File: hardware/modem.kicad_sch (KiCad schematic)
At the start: 33 parts, among them J11 PRPC001DAAN-RC, Q2 IRLML2246TRPBF, Q3 MMBT3904, U7 74AVC1T45DW-7, U8 74AVC1T45DW-7, U9 SARA-R500S-61B

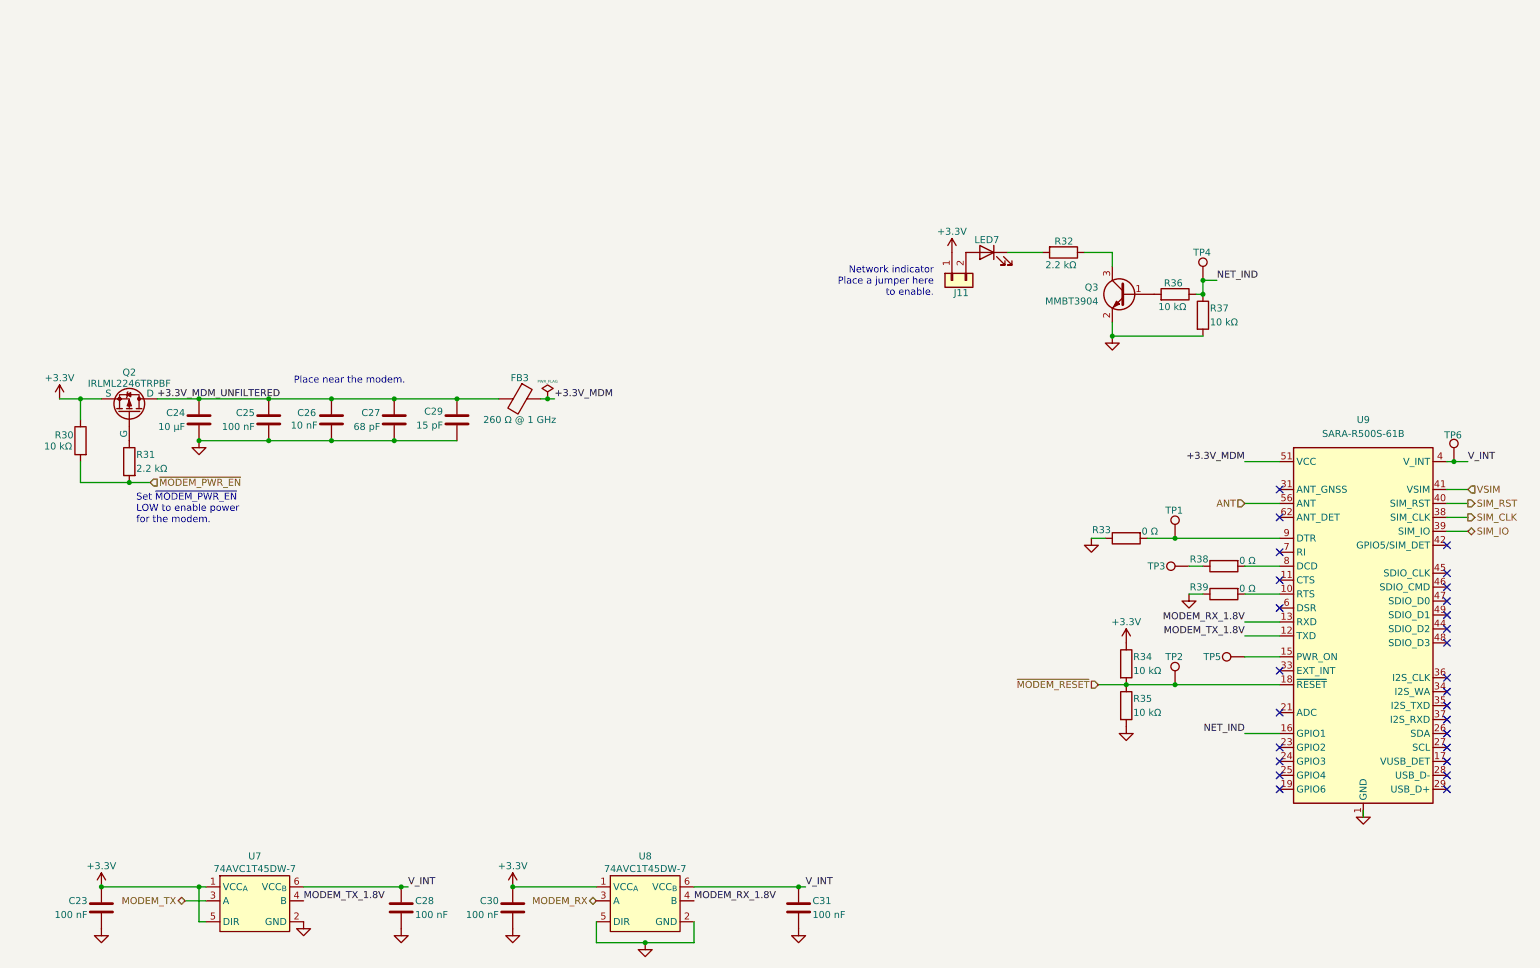
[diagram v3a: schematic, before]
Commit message: HW: Update components, change footprints to handsolder versions, finish power
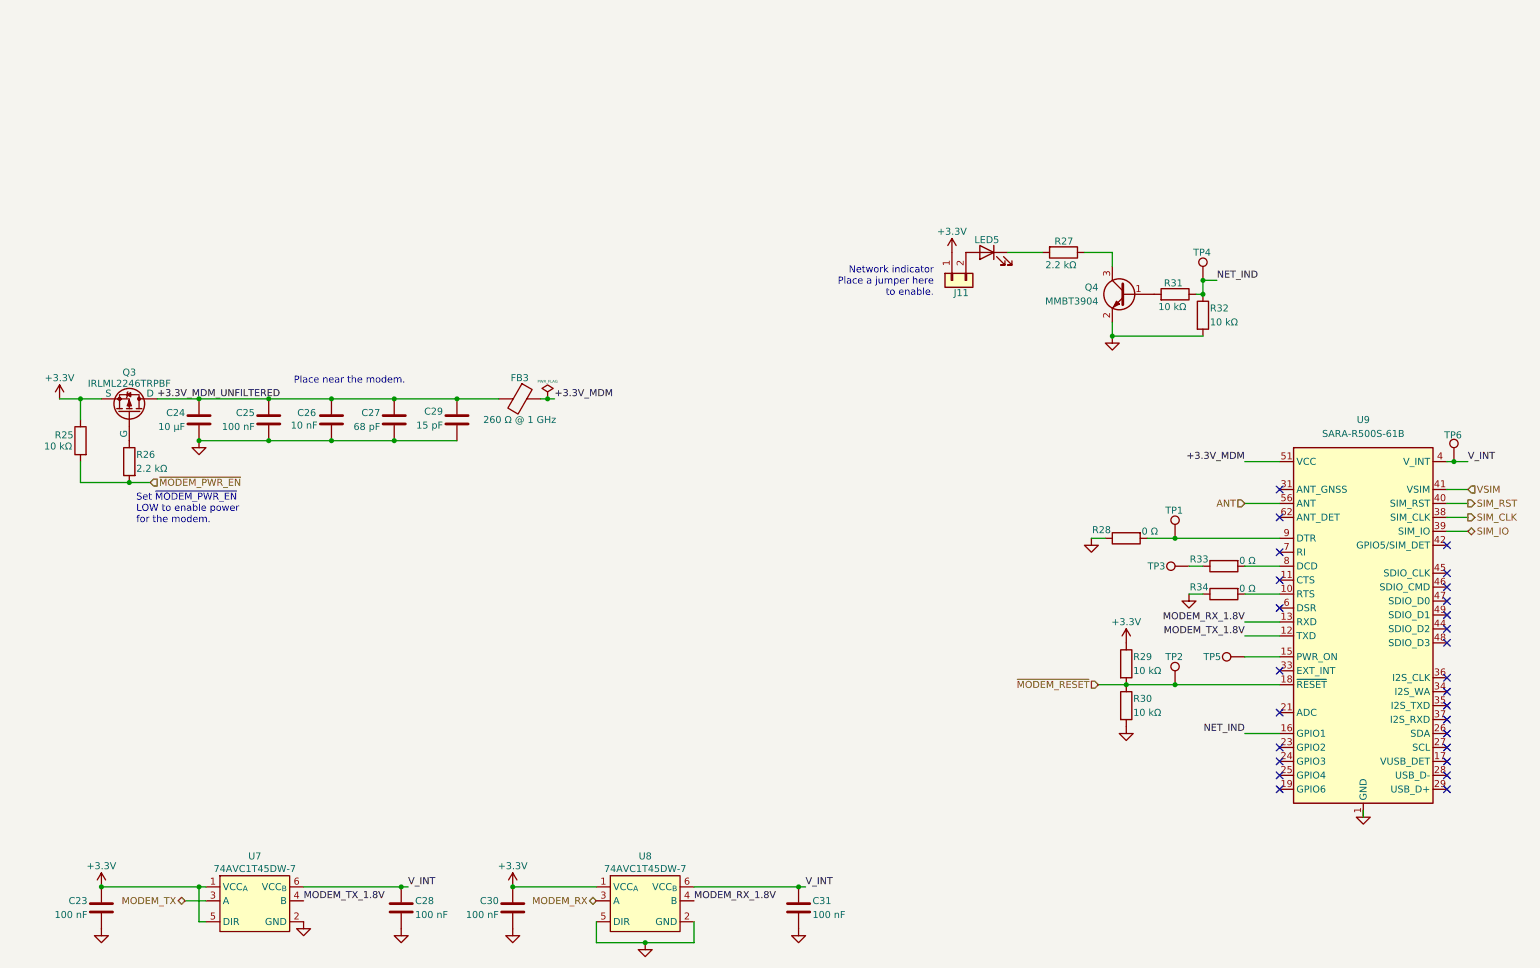
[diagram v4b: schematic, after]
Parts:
- R25: renamed from R30; Digi-Key Part Number 311-10.0KLRCT-ND -> 732-560112110020CT-ND; Manufacturer YAGEO -> Würth Elektronik; Manufacturer Part Number RC0402FR-0710KL -> 560112110020
- R26: renamed from R31; Digi-Key Part Number 311-2.20KLRCT-ND -> 732-560112110087CT-ND; Manufacturer YAGEO -> Würth Elektronik; Manufacturer Part Number RC0402FR-072K2L -> 560112110087
- R27: renamed from R32; Digi-Key Part Number 311-2.20KLRCT-ND -> 732-560112110087CT-ND; Manufacturer YAGEO -> Würth Elektronik; Manufacturer Part Number RC0402FR-072K2L -> 560112110087
- R28: renamed from R33; Digi-Key Part Number 311-0.0JRCT-ND -> 732-560112110001CT-ND; Manufacturer YAGEO -> Würth Elektronik; Manufacturer Part Number RC0402JR-070RL -> 560112110001
- R29: renamed from R34; Digi-Key Part Number 311-10.0KLRCT-ND -> 732-560112110020CT-ND; Manufacturer YAGEO -> Würth Elektronik; Manufacturer Part Number RC0402FR-0710KL -> 560112110020
- R30: renamed from R35; Digi-Key Part Number 311-10.0KLRCT-ND -> 732-560112110020CT-ND; Manufacturer YAGEO -> Würth Elektronik; Manufacturer Part Number RC0402FR-0710KL -> 560112110020
- R31: renamed from R36; Digi-Key Part Number 311-10.0KLRCT-ND -> 732-560112110020CT-ND; Manufacturer YAGEO -> Würth Elektronik; Manufacturer Part Number RC0402FR-0710KL -> 560112110020
- R32: renamed from R37; Digi-Key Part Number 311-10.0KLRCT-ND -> 732-560112110020CT-ND; Manufacturer YAGEO -> Würth Elektronik; Manufacturer Part Number RC0402FR-0710KL -> 560112110020
- R33: renamed from R38; Digi-Key Part Number 311-0.0JRCT-ND -> 732-560112110001CT-ND; Manufacturer YAGEO -> Würth Elektronik; Manufacturer Part Number RC0402JR-070RL -> 560112110001
- R34: renamed from R39; Digi-Key Part Number 311-0.0JRCT-ND -> 732-560112110001CT-ND; Manufacturer YAGEO -> Würth Elektronik; Manufacturer Part Number RC0402JR-070RL -> 560112110001
- renumbered LED7 to LED5, Q2 to Q3, Q3 to Q4

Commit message: HW: Add battery protection
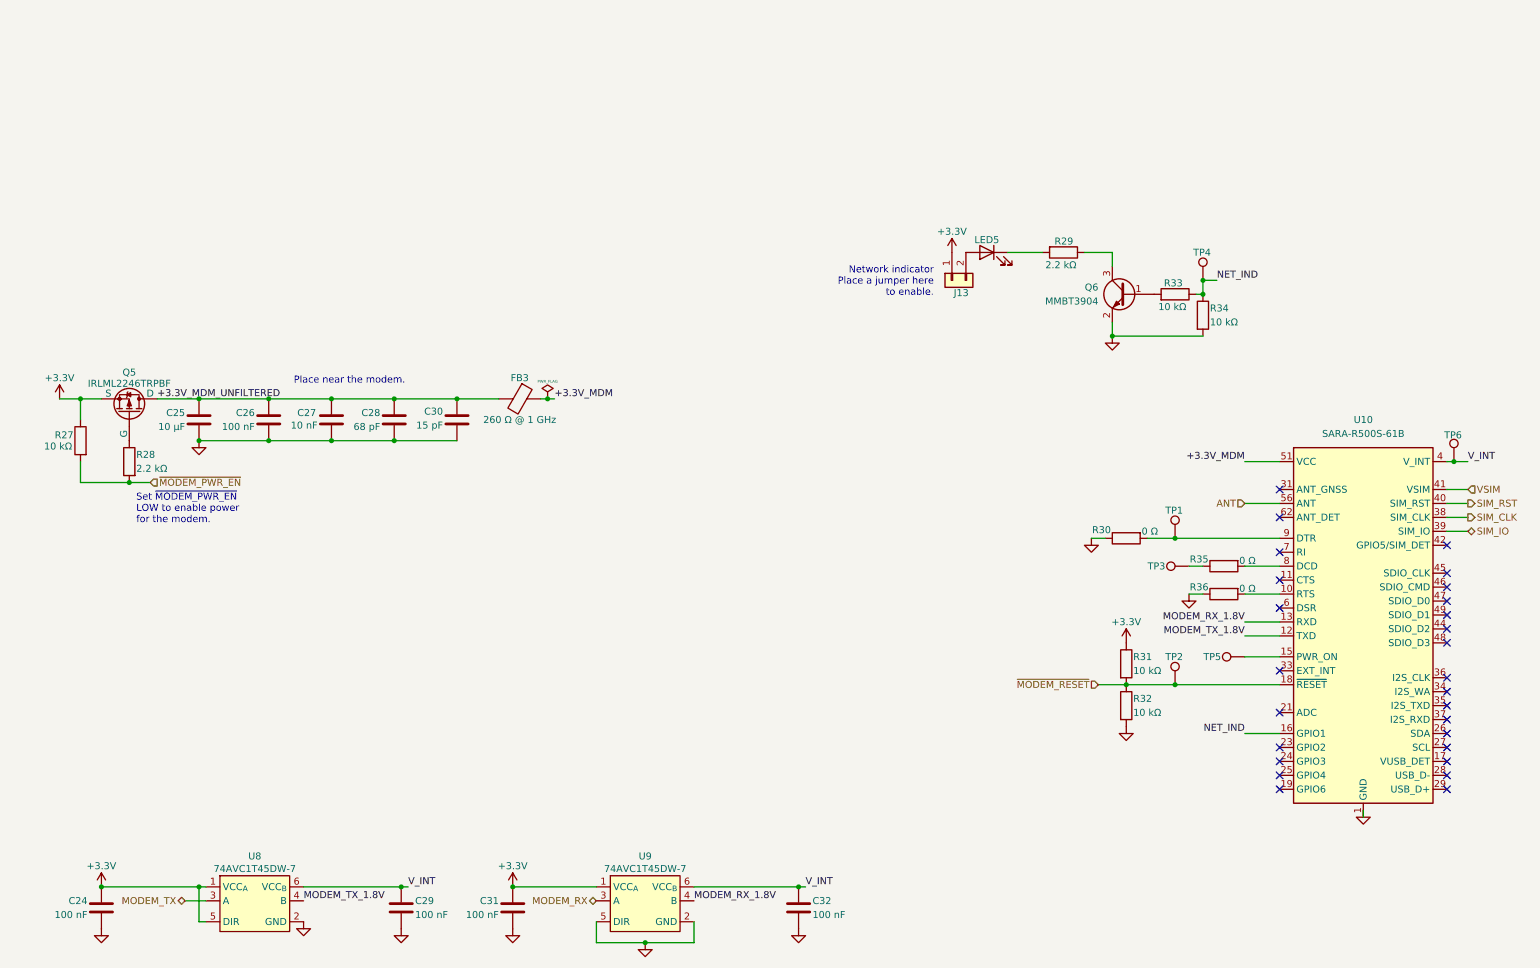
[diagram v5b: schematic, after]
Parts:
- renumbered C23 to C24, C24 to C25, C25 to C26, C26 to C27, C27 to C28, C28 to C29, C29 to C30, C30 to C31, C31 to C32, J11 to J13, Q3 to Q5, Q4 to Q6, R25 to R27, R26 to R28, R27 to R29, R28 to R30, R29 to R31, R30 to R32, R31 to R33, R32 to R34, R33 to R35, R34 to R36, U9 to U10, U7 to U8, U8 to U9

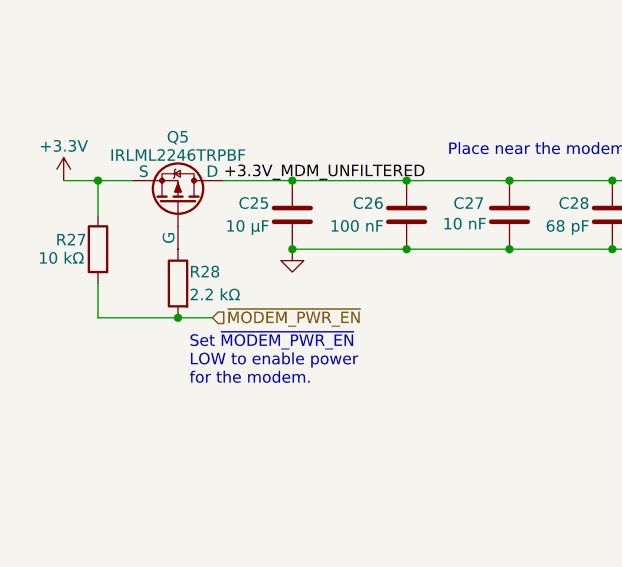
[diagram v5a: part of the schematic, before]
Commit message: HW: Resize modem power fet gate resistor
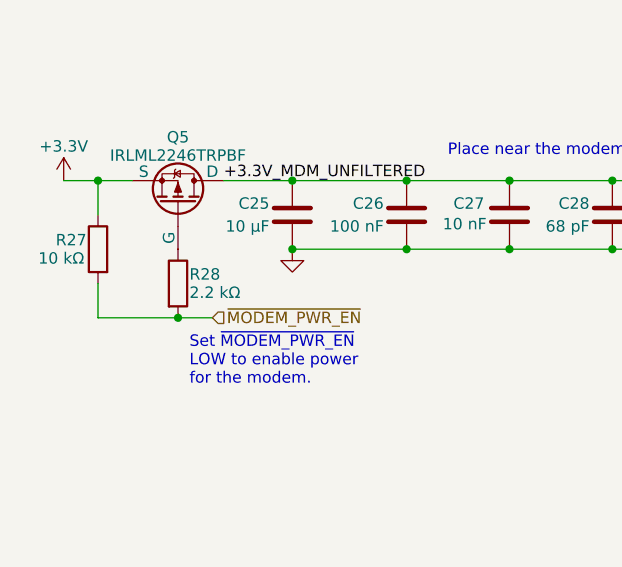
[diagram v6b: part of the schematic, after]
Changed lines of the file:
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@@
 	)
 	(junction
-		(at 30.48 102.87)
-		(diameter 0)
-		(color 0 0 0 0)
-	)
-	(junction
 		(at 226.06 68.58)
 		(diameter 0)
@@
 	)
 	(junction
+		(at 30.48 102.87)
+		(diameter 0)
+		(color 0 0 0 0)
+	)
+	(junction
 		(at 100.33 176.53)
 		(diameter 0)
@@
 	(wire
 		(pts
+			(xy 30.48 102.87) (xy 34.29 102.87)
+		)
+		(stroke
+			(width 0)
+			(type default)
+		)
+	)
+	(wire
+		(pts
 			(xy 80.01 176.53) (xy 81.28 176.53)
 		)
@@
 	(wire
 		(pts
-			(xy 30.48 102.87) (xy 34.29 102.87)
-		)
-		(stroke
-			(width 0)
-			(type default)
-		)
-	)
-	(wire
-		(pts
 			(xy 270.51 106.68) (xy 274.32 106.68)
 		)
@@
 	)
 	(symbol
+		(lib_id "Device:R")
+		(at 30.48 99.06 0)
+		(unit 1)
+		(exclude_from_sim no)
+		(in_bom yes)
+		(on_board yes)
+		(dnp no)
+		(property "Reference" "R28"
+			(at 31.75 98.044 0)
+			(effects
+				(font
+					(size 1.27 1.27)
+				)
+				(justify left)
+			)
+		)
+		(property "Value" "2.2 kΩ"
+			(at 31.75 100.076 0)
+			(effects
+				(font
+					(size 1.27 1.27)
+				)
+				(justify left)
+			)
+		)
+		(property "Footprint" "Resistor_SMD:R_0402_1005Metric_Pad0.72x0.64mm_HandSolder"
+			(at 28.702 99.06 90)
+			(effects
+				(font
+					(size 1.27 1.27)
+				)
+				(hide yes)
+			)
+		)
+		(property "Datasheet" "~"
+			(at 30.48 99.06 0)
+			(effects
+				(font
+					(size 1.27 1.27)
+				)
+				(hide yes)
+			)
+		)
+		(property "Description" ""
+			(at 30.48 99.06 0)
+			(effects
+				(font
+					(size 1.27 1.27)
+				)
+				(hide yes)
+			)
+		)
+		(property "Digi-Key Part Number" "732-560112110087CT-ND"
+			(at 30.48 99.06 0)
+			(effects
+				(font
+					(size 1.27 1.27)
+				)
+				(hide yes)
+			)
+		)
+		(property "Manufacturer" "Würth Elektronik"
+			(at 30.48 99.06 0)
+			(effects
+				(font
+					(size 1.27 1.27)
+				)
+				(hide yes)
+			)
+		)
+		(property "Manufacturer Part Number" "560112110087"
+			(at 30.48 99.06 0)
+			(effects
+				(font
+					(size 1.27 1.27)
+				)
+				(hide yes)
+			)
+		)
+		(pin "2"
+		)
+		(pin "1"
+		)
+		(instances
+			(project "iida_devkit"
+				(path "/b12a6e25-97fb-4aba-bc96-af8db389bb9a/3723475b-e956-4027-ac40-e47346743900"
+					(reference "R28")
+					(unit 1)
+				)
+			)
+		)
+	)
+	(symbol
 		(lib_id "Connector:TestPoint")
 		(at 226.06 66.04 0)
@@
 					(unit 1)
 				)
-			)
-		)
-	)
-	(symbol
-		(lib_id "Device:R")
-		(at 30.48 99.06 0)
-		(mirror y)
-		(unit 1)
-		(exclude_from_sim no)
-		(in_bom yes)
-		(on_board yes)
-		(dnp no)
-		(property "Reference" "R28"
-			(at 31.75 97.79 0)
-			(effects
-				(font
-					(size 1.27 1.27)
-				)
-				(justify right)
-			)
-		)
-		(property "Value" "2.2 kΩ"
-			(at 31.75 100.33 0)
-			(effects
-				(font
-					(size 1.27 1.27)
-				)
-				(justify right)
-			)
-		)
-		(property "Footprint" "Resistor_SMD:R_0402_1005Metric_Pad0.72x0.64mm_HandSolder"
-			(at 32.258 99.06 90)
-			(effects
-				(font
-					(size 1.27 1.27)
-				)
-				(hide yes)
-			)
-		)
-		(property "Datasheet" "~"
-			(at 30.48 99.06 0)
-			(effects
-				(font
-					(size 1.27 1.27)
-				)
-				(hide yes)
-			)
-		)
-		(property "Description" ""
-			(at 30.48 99.06 0)
-			(effects
-				(font
-					(size 1.27 1.27)
-				)
-				(hide yes)
-			)
-		)
-		(property "Digi-Key Part Number" "732-560112110087CT-ND"
-			(at 30.48 99.06 0)
-			(effects
-				(font
-					(size 1.27 1.27)
-				)
-				(hide yes)
-			)
-		)
-		(property "Manufacturer" "Würth Elektronik"
-			(at 30.48 99.06 0)
-			(effects
-				(font
-					(size 1.27 1.27)
-				)
-				(hide yes)
-			)
-		)
-		(property "Manufacturer Part Number" "560112110087"
-			(at 30.48 99.06 0)
-			(effects
-				(font
-					(size 1.27 1.27)
-				)
-				(hide yes)
-			)
-		)
-		(pin "2"
-		)
-		(pin "1"
-		)
-		(instances
-			(project "iida_devkit"
-				(path "/b12a6e25-97fb-4aba-bc96-af8db389bb9a/3723475b-e956-4027-ac40-e47346743900"
-					(reference "R28")
-					(unit 1)
-				)
